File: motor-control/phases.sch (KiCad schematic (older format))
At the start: 42 parts, among them Q1 csd19505kcs, Q10 csd19505kcs, Q11 csd19505kcs, Q12 csd19505kcs, Q2 csd19505kcs, Q3 csd19505kcs, Q4 csd19505kcs, Q5 csd19505kcs, Q6 csd19505kcs, Q7 csd19505kcs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

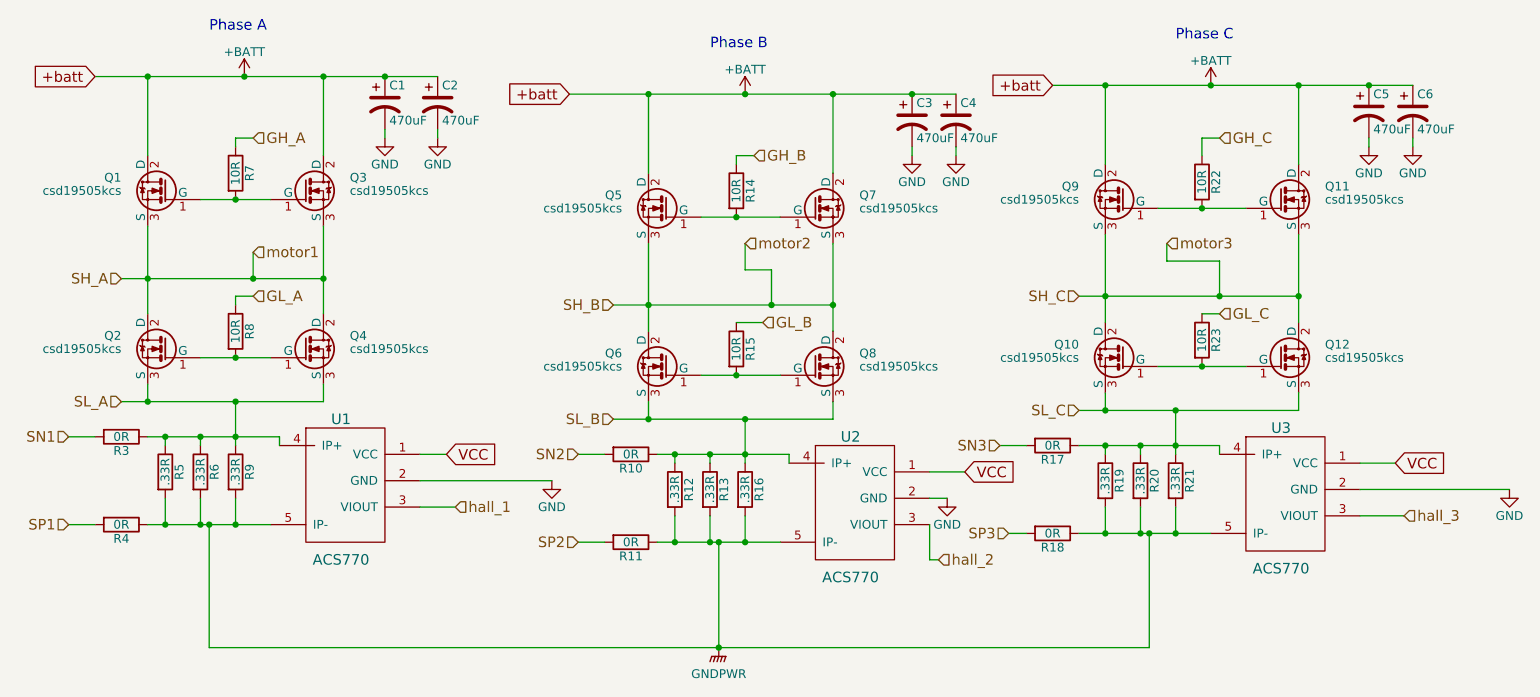
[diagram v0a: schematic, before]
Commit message: Added hall filtering/bypass, part #s, associations
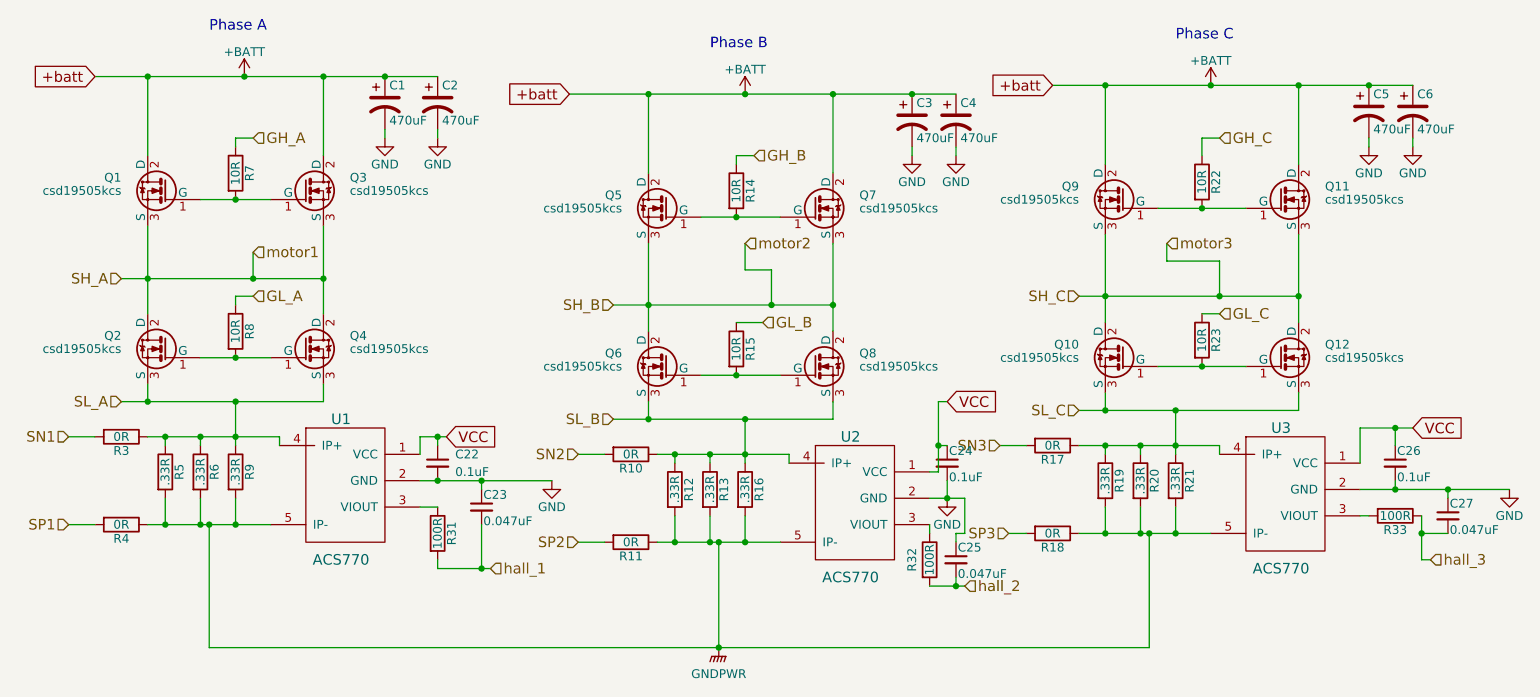
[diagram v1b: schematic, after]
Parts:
- added C22, C24, C26: 0.1uF, Capacitors_SMD:C_0805, symbol C_Small
- added C23, C25, C27: 0.047uF, Capacitors_SMD:C_0805, symbol C_Small
- added R31, R32, R33: 100R, Resistors_SMD:R_0805, symbol R
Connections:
- net GND: now also C22.2, C23.1, C24.2, C25.1, C26.2, C27.1
- net VCC: now also C22.1, C24.1, C26.1
- net hall_1: now also C23.2, R31.2; no longer U1.3 (VIOUT)
- net hall_2: now also C25.2, R32.2; no longer U2.3 (VIOUT)
- net hall_3: now also C27.2, R33.1; no longer U3.3 (VIOUT)
- new net: R31.1, U1.3 (VIOUT)
- new net: R32.1, U2.3 (VIOUT)
- new net: R33.2, U3.3 (VIOUT)
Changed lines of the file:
@@
 	6550 4600 6550 5200
 Connection ~ 6550 5200
-Text GLabel 5000 4100 2    60   Input ~ 0
+Text GLabel 5000 4000 2    60   Input ~ 0
 VCC
-Text GLabel 7950 4200 2    60   Input ~ 0
+Text GLabel 7850 3800 2    60   Input ~ 0
 VCC
-Text GLabel 10400 4150 2    60   Input ~ 0
+Text GLabel 10500 3950 2    60   Input ~ 0
 VCC
-Wire Wire Line
-	5000 4100 4850 4100
-Wire Wire Line
-	7750 4200 7950 4200
-Wire Wire Line
-	10200 4150 10400 4150
-Text HLabel 5050 4400 2    60   Input ~ 0
+Text HLabel 5250 4750 2    60   Input ~ 0
 hall_1
-Text HLabel 7800 4700 2    60   Input ~ 0
+Text HLabel 7950 4850 2    60   Input ~ 0
 hall_2
-Text HLabel 10450 4450 2    60   Input ~ 0
+Text HLabel 10600 4700 2    60   Input ~ 0
 hall_3
 $Comp
@@
 	1    0    0    -1
 $EndComp
-Wire Wire Line
-	4850 4400 5050 4400
-Wire Wire Line
-	10200 4450 10450 4450
-Wire Wire Line
-	4850 4250 5600 4250
 $Comp
 L GND #PWR015
@@
 SP3
 Wire Wire Line
-	7800 4700 7750 4700
-Wire Wire Line
-	7750 4700 7750 4500
-Wire Wire Line
-	7850 4350 7750 4350
+	7750 4350 7950 4350
 Connection ~ 8750 4050
 Wire Wire Line
@@
 Wire Wire Line
 	10500 2350 10500 2300
+$Comp
+L C_Small C22
+U 1 1 56B30753
+P 4950 4150
+F 0 "C22" H 5050 4200 50  0000 L CNN
+F 1 "0.1uF" H 5050 4100 50  0000 L CNN
+F 2 "Capacitors_SMD:C_0805" H 4950 4150 50  0001 C CNN
+F 3 "http://www.mouser.com/ProductDetail/Kemet/C0805C104K3RACTU/?qs=sGAEpiMZZMsh%252b1woXyUXjy2nLb0oGP6S1b6VKwFAUBM%3d" H 4950 4150 50  0001 C CNN
+	1    4950 4150
+	1    0    0    -1
+$EndComp
+Wire Wire Line
+	4850 4250 5600 4250
+Connection ~ 4950 4250
+Wire Wire Line
+	4850 4100 4850 4000
+Wire Wire Line
+	4850 4000 5000 4000
+Wire Wire Line
+	4950 4050 4950 4000
+Connection ~ 4950 4000
+$Comp
+L C_Small C23
+U 1 1 56B31DA0
+P 5200 4400
+F 0 "C23" H 5210 4470 50  0000 L CNN
+F 1 "0.047uF" H 5210 4320 50  0000 L CNN
+F 2 "Capacitors_SMD:C_0805" H 5200 4400 50  0001 C CNN
+F 3 "http://www.mouser.com/ProductDetail/AVX/0805YC473KAT2A/?qs=sGAEpiMZZMs0AnBnWHyRQKG%2f91LbtRSiVF39sFx40v8%3d" H 5200 4400 50  0001 C CNN
+	1    5200 4400
+	1    0    0    -1
+$EndComp
+$Comp
+L C_Small C25
+U 1 1 56B324F9
+P 7900 4700
+F 0 "C25" H 7910 4770 50  0000 L CNN
+F 1 "0.047uF" H 7910 4620 50  0000 L CNN
+F 2 "Capacitors_SMD:C_0805" H 7900 4700 50  0001 C CNN
+F 3 "http://www.mouser.com/ProductDetail/AVX/0805YC473KAT2A/?qs=sGAEpiMZZMs0AnBnWHyRQKG%2f91LbtRSiVF39sFx40v8%3d" H 7900 4700 50  0001 C CNN
+	1    7900 4700
+	1    0    0    -1
+$EndComp
+$Comp
+L C_Small C24
+U 1 1 56B32576
+P 7850 4150
+F 0 "C24" H 7860 4220 50  0000 L CNN
+F 1 "0.1uF" H 7860 4070 50  0000 L CNN
+F 2 "Capacitors_SMD:C_0805" H 7850 4150 50  0001 C CNN
+F 3 "http://www.mouser.com/ProductDetail/Kemet/C0805C104K3RACTU/?qs=sGAEpiMZZMsh%252b1woXyUXjy2nLb0oGP6S1b6VKwFAUBM%3d" H 7850 4150 50  0001 C CNN
+	1    7850 4150
+	1    0    0    -1
+$EndComp
+$Comp
+L C_Small C26
+U 1 1 56B32AFB
+P 10400 4150
+F 0 "C26" H 10410 4220 50  0000 L CNN
+F 1 "0.1uF" H 10410 4070 50  0000 L CNN
+F 2 "Capacitors_SMD:C_0805" H 10400 4150 50  0001 C CNN
+F 3 "http://www.mouser.com/ProductDetail/Kemet/C0805C104K3RACTU/?qs=sGAEpiMZZMsh%252b1woXyUXjy2nLb0oGP6S1b6VKwFAUBM%3d" H 10400 4150 50  0001 C CNN
+	1    10400 4150
+	1    0    0    -1
+$EndComp
+$Comp
+L C_Small C27
+U 1 1 56B32B86
+P 10700 4450
+F 0 "C27" H 10710 4520 50  0000 L CNN
+F 1 "0.047uF" H 10710 4370 50  0000 L CNN
+F 2 "Capacitors_SMD:C_0805" H 10700 4450 50  0001 C CNN
+F 3 "http://www.mouser.com/ProductDetail/AVX/0805YC473KAT2A/?qs=sGAEpiMZZMs0AnBnWHyRQKG%2f91LbtRSiVF39sFx40v8%3d" H 10700 4450 50  0001 C CNN
+	1    10700 4450
+	1    0    0    -1
+$EndComp
+$Comp
+L R R31
+U 1 1 56B33573
+P 4950 4550
+F 0 "R31" V 5030 4550 50  0000 C CNN
+F 1 "100R" V 4950 4550 50  0000 C CNN
+F 2 "Resistors_SMD:R_0805" V 4880 4550 50  0001 C CNN
+F 3 "http://www.mouser.com/ProductDetail/Bourns/CRS0805-FX-1000ELF/?qs=sGAEpiMZZMtlubZbdhIBIE4X4CLDUFJw6OTs2jsUdzw%3d" H 4950 4550 50  0001 C CNN
+	1    4950 4550
+	1    0    0    -1
+$EndComp
+$Comp
+L R R32
+U 1 1 56B345B9
+P 7750 4700
+F 0 "R32" V 7650 4700 50  0000 C CNN
+F 1 "100R" V 7750 4700 50  0000 C CNN
+F 2 "Resistors_SMD:R_0805" V 7680 4700 50  0001 C CNN
+F 3 "http://www.mouser.com/ProductDetail/Bourns/CRS0805-FX-1000ELF/?qs=sGAEpiMZZMtlubZbdhIBIE4X4CLDUFJw6OTs2jsUdzw%3d" H 7750 4700 50  0001 C CNN
+	1    7750 4700
+	1    0    0    -1
+$EndComp
+$Comp
+L R R33
+U 1 1 56B34890
+P 10400 4450
+F 0 "R33" V 10480 4450 50  0000 C CNN
+F 1 "100R" V 10400 4450 50  0000 C CNN
+F 2 "Resistors_SMD:R_0805" V 10330 4450 50  0001 C CNN
+F 3 "http://www.mouser.com/ProductDetail/Bourns/CRS0805-FX-1000ELF/?qs=sGAEpiMZZMtlubZbdhIBIE4X4CLDUFJw6OTs2jsUdzw%3d" H 10400 4450 50  0001 C CNN
+	1    10400 4450
+	0    1    1    0
+$EndComp
+Wire Wire Line
+	4950 4700 4950 4750
+Wire Wire Line
+	4950 4750 5250 4750
+Wire Wire Line
+	5200 4500 5200 4750
+Connection ~ 5200 4750
+Wire Wire Line
+	5200 4300 5200 4250
+Connection ~ 5200 4250
+Wire Wire Line
+	4850 4400 4950 4400
+Wire Wire Line
+	7850 3800 7800 3800
+Wire Wire Line
+	7800 3800 7800 4200
+Wire Wire Line
+	7800 4200 7750 4200
+Wire Wire Line
+	7850 4050 7800 4050
+Connection ~ 7800 4050
+Wire Wire Line
+	7850 4250 7850 4350
+Connection ~ 7850 4350
+Wire Wire Line
+	7900 4600 7900 4550
+Wire Wire Line
+	7900 4550 7950 4550
+Wire Wire Line
+	7950 4550 7950 4350
+Wire Wire Line
+	7750 4550 7750 4500
+Wire Wire Line
+	7750 4850 7950 4850
+Wire Wire Line
+	7900 4850 7900 4800
+Connection ~ 7900 4850
+Wire Wire Line
+	10500 3950 10200 3950
+Wire Wire Line
+	10200 3950 10200 4150
+Wire Wire Line
+	10400 4050 10400 3950
+Connection ~ 10400 3950
+Wire Wire Line
+	10400 4250 10400 4300
+Connection ~ 10400 4300
+Wire Wire Line
+	10700 4350 10700 4300
+Connection ~ 10700 4300
+Wire Wire Line
+	10550 4450 10550 4700
+Wire Wire Line
+	10550 4550 10700 4550
+Wire Wire Line
+	10200 4450 10250 4450
+Wire Wire Line
+	10550 4700 10600 4700
+Connection ~ 10550 4550
 $EndSCHEMATC
